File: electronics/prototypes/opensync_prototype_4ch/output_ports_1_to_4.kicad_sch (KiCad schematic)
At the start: 24 parts, among them J4 61611042121502, J5 61611042121502, J6 61611042121502, J7 61611042121502, U5 SN74LVC1T45DCKR, U6 SN74LVC1T45DCKR, U7 SN74LVC1T45DCKR, U8 SN74LVC1T45DCKR

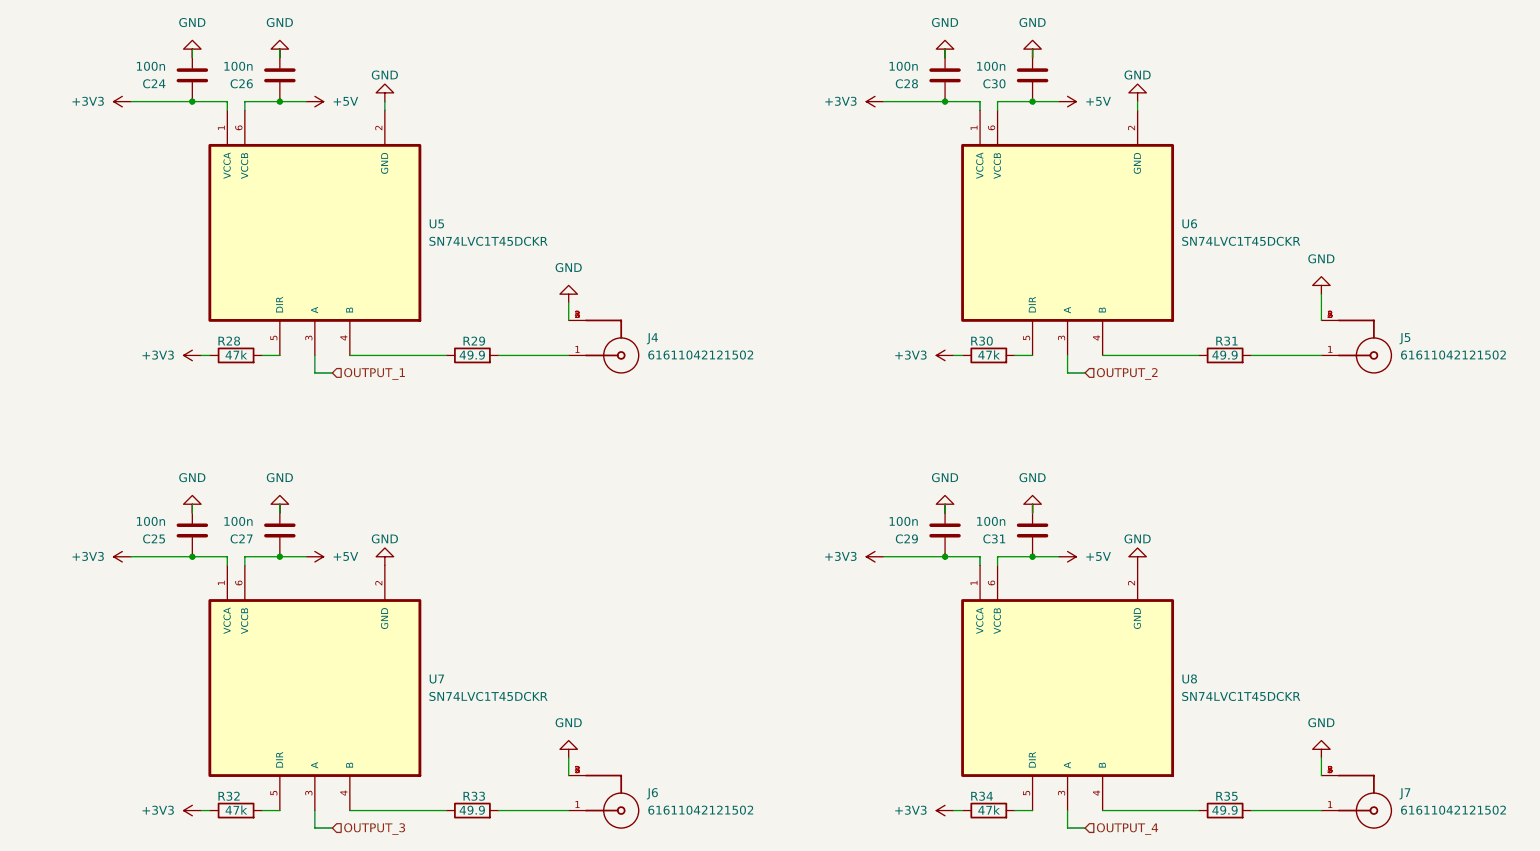
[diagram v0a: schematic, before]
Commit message: Added part numbers
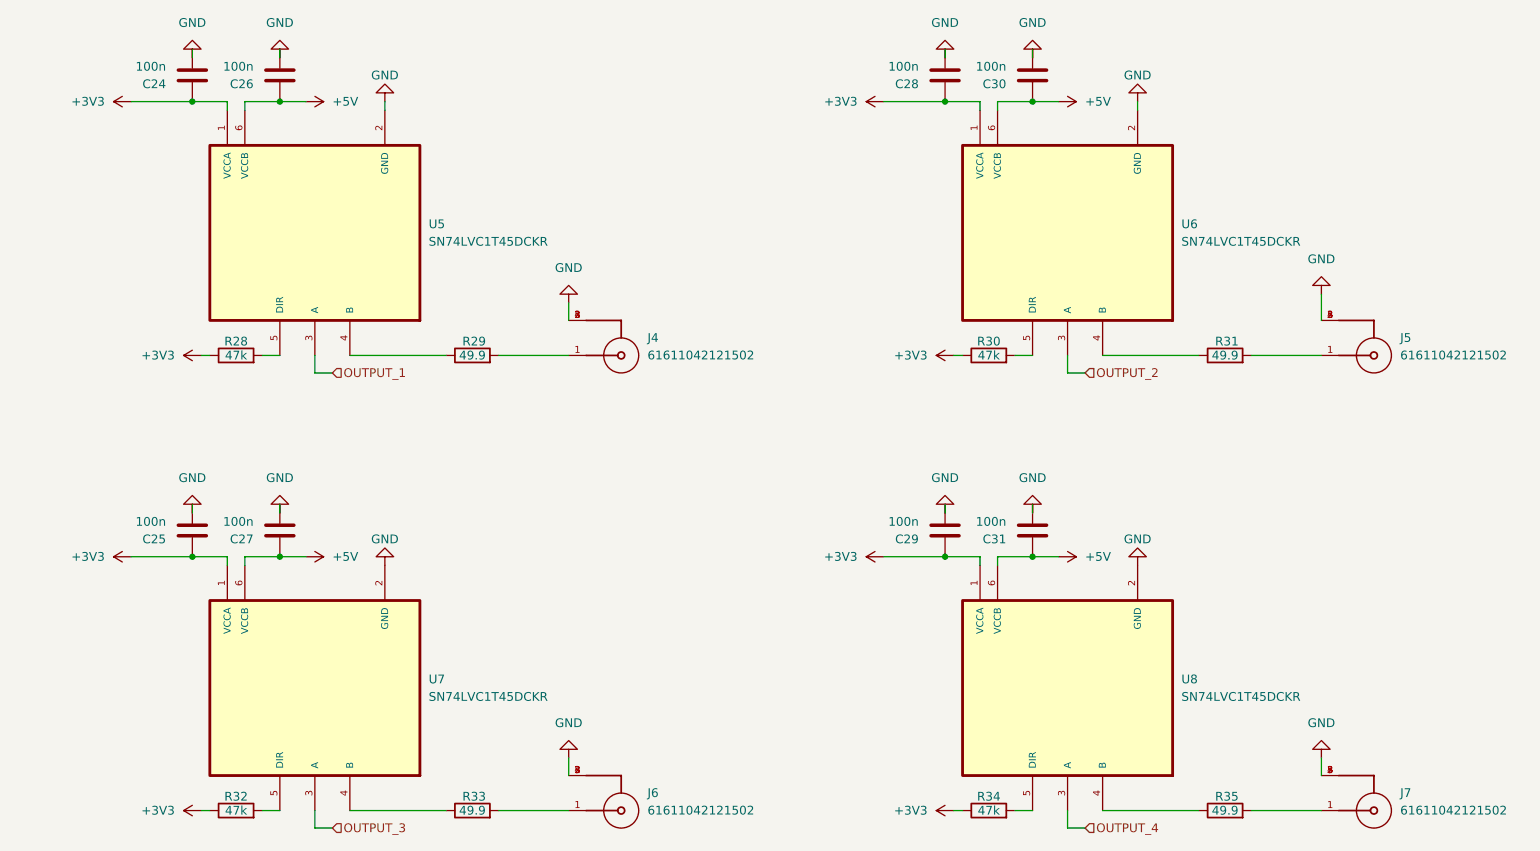
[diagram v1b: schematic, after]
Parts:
- C24, C25, C26, C27, C28, C29, C30, C31: LCSC (none) -> C60474
- R28, R30, R32, R34: LCSC (none) -> C176117
- R29, R31, R33, R35: LCSC (none) -> C1858992
- U5, U6, U7, U8: LCSC (none) -> C9382
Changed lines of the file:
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@@
 			)
 		)
+		(property "LCSC" "C1858992"
+			(at 209.55 151.13 0)
+			(effects
+				(font
+					(size 1.27 1.27)
+				)
+				(hide yes)
+			)
+		)
 		(pin "2"
 		)
@@
 			)
 		)
+		(property "LCSC" "C60474"
+			(at 168.91 44.45 0)
+			(effects
+				(font
+					(size 1.27 1.27)
+				)
+				(hide yes)
+			)
+		)
 		(pin "1"
 		)
@@
 			)
 		)
+		(property "LCSC" "C60474"
+			(at 168.91 110.49 0)
+			(effects
+				(font
+					(size 1.27 1.27)
+				)
+				(hide yes)
+			)
+		)
 		(pin "1"
 		)
@@
 			)
 		)
+		(property "LCSC" ""
+			(at 121.92 85.09 0)
+			(effects
+				(font
+					(size 1.27 1.27)
+				)
+			)
+		)
 		(pin "4"
 		)
@@
 			)
 		)
+		(property "LCSC" "C9382"
+			(at 77.47 67.31 0)
+			(effects
+				(font
+					(size 1.27 1.27)
+				)
+				(hide yes)
+			)
+		)
 		(pin "1"
 		)
@@
 			)
 		)
+		(property "LCSC" "C60474"
+			(at 59.69 44.45 0)
+			(effects
+				(font
+					(size 1.27 1.27)
+				)
+				(hide yes)
+			)
+		)
 		(pin "1"
 		)
@@
 		(dnp no)
 		(property "Reference" "R32"
-			(at 65.024 149.098 90)
+			(at 66.04 149.098 90)
 			(effects
 				(font
@@
 			)
 		)
+		(property "LCSC" "C176117"
+			(at 66.04 151.13 0)
+			(effects
+				(font
+					(size 1.27 1.27)
+				)
+				(hide yes)
+			)
+		)
 		(pin "1"
 		)
@@
 			)
 		)
+		(property "LCSC" ""
+			(at 121.92 151.13 0)
+			(effects
+				(font
+					(size 1.27 1.27)
+				)
+			)
+		)
 		(pin "4"
 		)
@@
 			)
 		)
+		(property "LCSC" "C60474"
+			(at 72.39 44.45 0)
+			(effects
+				(font
+					(size 1.27 1.27)
+				)
+				(hide yes)
+			)
+		)
 		(pin "1"
 		)
@@
 			)
 		)
+		(property "LCSC" "C1858992"
+			(at 209.55 85.09 0)
+			(effects
+				(font
+					(size 1.27 1.27)
+				)
+				(hide yes)
+			)
+		)
 		(pin "2"
 		)
@@
 			)
 		)
+		(property "LCSC" ""
+			(at 231.14 151.13 0)
+			(effects
+				(font
+					(size 1.27 1.27)
+				)
+			)
+		)
 		(pin "4"
 		)
@@
 			)
 		)
+		(property "LCSC" "C9382"
+			(at 186.69 67.31 0)
+			(effects
+				(font
+					(size 1.27 1.27)
+				)
+				(hide yes)
+			)
+		)
 		(pin "1"
 		)
@@
 			)
 		)
+		(property "LCSC" "C9382"
+			(at 186.69 133.35 0)
+			(effects
+				(font
+					(size 1.27 1.27)
+				)
+				(hide yes)
+			)
+		)
 		(pin "1"
 		)
@@
 		(dnp no)
 		(property "Reference" "R34"
-			(at 174.244 149.098 90)
+			(at 175.26 149.098 90)
 			(effects
 				(font
@@
 			)
 		)
+		(property "LCSC" "C176117"
+			(at 175.26 151.13 0)
+			(effects
+				(font
+					(size 1.27 1.27)
+				)
+				(hide yes)
+			)
+		)
 		(pin "1"
 		)
@@
 			)
 		)
+		(property "LCSC" "C60474"
+			(at 181.61 44.45 0)
+			(effects
+				(font
+					(size 1.27 1.27)
+				)
+				(hide yes)
+			)
+		)
 		(pin "1"
 		)
@@
 			)
 		)
+		(property "LCSC" "C60474"
+			(at 181.61 110.49 0)
+			(effects
+				(font
+					(size 1.27 1.27)
+				)
+				(hide yes)
+			)
+		)
 		(pin "1"
 		)
@@
 			)
 		)
+		(property "LCSC" "C60474"
+			(at 72.39 110.49 0)
+			(effects
+				(font
+					(size 1.27 1.27)
+				)
+				(hide yes)
+			)
+		)
 		(pin "1"
 		)
@@
 			)
 		)
+		(property "LCSC" "C1858992"
+			(at 100.33 85.09 0)
+			(effects
+				(font
+					(size 1.27 1.27)
+				)
+				(hide yes)
+			)
+		)
 		(pin "2"
 		)
@@
 			)
 		)
+		(property "LCSC" "C60474"
+			(at 59.69 110.49 0)
+			(effects
+				(font
+					(size 1.27 1.27)
+				)
+				(hide yes)
+			)
+		)
 		(pin "1"
 		)
@@
 			)
 		)
+		(property "LCSC" ""
+			(at 231.14 85.09 0)
+			(effects
+				(font
+					(size 1.27 1.27)
+				)
+			)
+		)
 		(pin "4"
 		)
@@
 		(dnp no)
 		(property "Reference" "R28"
-			(at 65.024 83.058 90)
+			(at 66.04 83.058 90)
 			(effects
 				(font
@@
 			)
 		)
+		(property "LCSC" "C176117"
+			(at 66.04 85.09 0)
+			(effects
+				(font
+					(size 1.27 1.27)
+				)
+				(hide yes)
+			)
+		)
 		(pin "1"
 		)
@@
 			)
 		)
+		(property "LCSC" "C1858992"
+			(at 100.33 151.13 0)
+			(effects
+				(font
+					(size 1.27 1.27)
+				)
+				(hide yes)
+			)
+		)
 		(pin "2"
 		)
@@
 		(dnp no)
 		(property "Reference" "R30"
-			(at 174.244 83.058 90)
+			(at 175.26 83.058 90)
 			(effects
 				(font
@@
 			)
 		)
+		(property "LCSC" "C176117"
+			(at 175.26 85.09 0)
+			(effects
+				(font
+					(size 1.27 1.27)
+				)
+				(hide yes)
+			)
+		)
 		(pin "1"
 		)
@@
 			(at 77.47 133.35 0)
 			(effects
+				(font
+					(size 1.27 1.27)
+				)
+				(hide yes)
+			)
+		)
+		(property "LCSC" "C9382"
+			(at 77.47 133.35 0)
+			(effects

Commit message: More prototyping
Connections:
- net +3V3: now also C24.2, C25.2, C28.2, C29.2; no longer C24.1, C25.1, C28.1, C29.1
- net +5V: now also C26.2, C27.2, C31.2; no longer C26.1, C27.1, C31.1
- net GND: now also C24.1, C25.1, C26.1, C27.1, C28.1, C29.1, C31.1; no longer C24.2, C25.2, C26.2, C27.2, C28.2, C29.2, C31.2
- net at R35.1: now also J7.1; no longer U8.4 (B)
- net at R35.2: now also U8.4 (B); no longer J7.1
- net at R31.1: now also J5.1; no longer U6.4 (B)
- net at R31.2: now also U6.4 (B); no longer J5.1
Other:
- moved on the sheet: C24, C25, C26, C27, C28, C29, C30, C31, J4, J5, J6, J7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
